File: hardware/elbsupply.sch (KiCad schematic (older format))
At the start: 82 parts, among them CON1 AVR-ISP-6, IC1 ATMEGA8-AI, P1 OUT_POS, P2 OUT_GND, P3 POWER_IN, Q1 KST2907A, SW1 SW_L, SW2 SW_R, SW3 SW_OE, SW4 SW_MD, U1 LM393, U2 TPS54331DDA, U3 LT1490, U4 LM358, U5 TS78L05CS, U6 LT3083

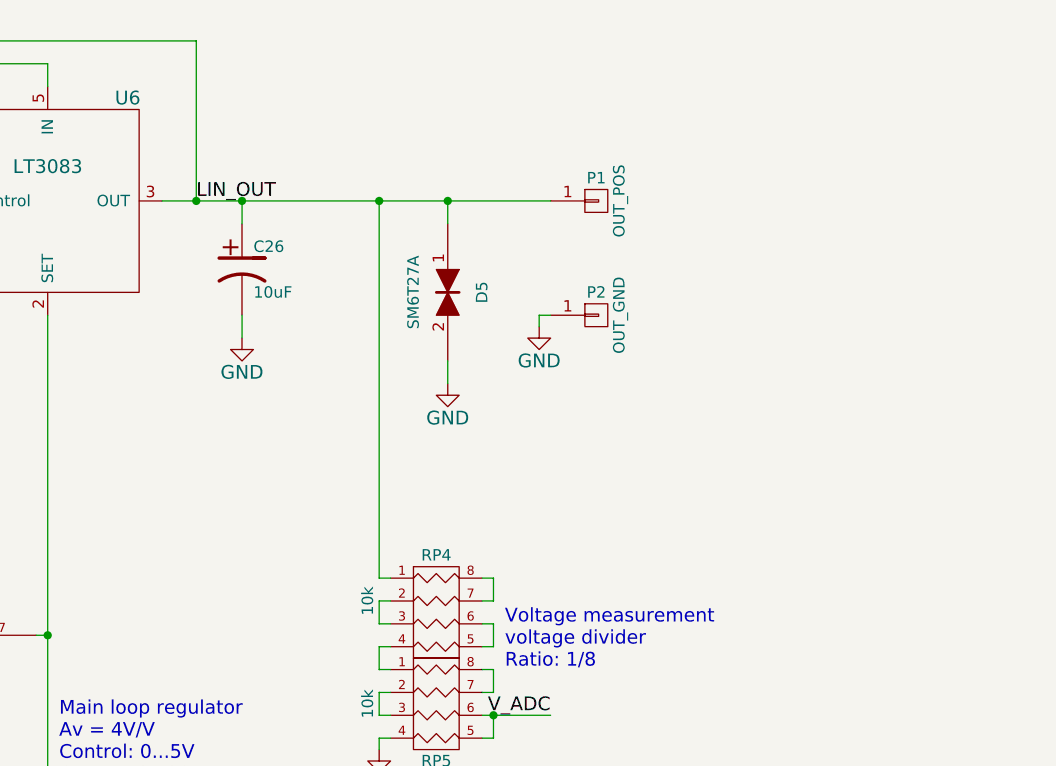
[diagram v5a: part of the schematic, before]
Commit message: quickly added LM334 constant current sink to ensure stable operation of LT3083
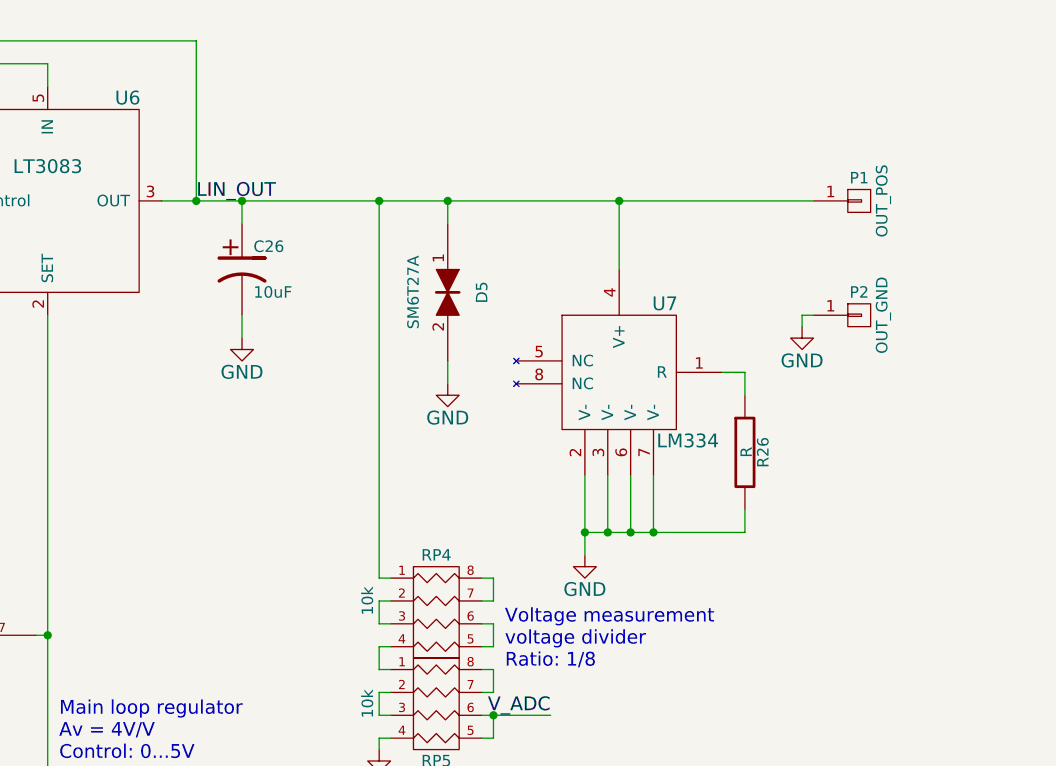
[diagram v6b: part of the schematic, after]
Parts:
- added R26: R, Resistors_SMD:R_0603_HandSoldering, symbol R
- added U7: LM334, devthrash_KICAD:SO8, symbol LM334
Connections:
- net GND: now also R26.2, U7.2 (V-), U7.3 (V-), U7.6 (V-), U7.7 (V-)
- net LIN_OUT: now also U7.4 (V+)
- new net: R26.1, U7.1 (R)
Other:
- moved on the sheet: P1, P2
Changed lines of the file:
@@
 LIBS:lt3083
 LIBS:tps54331dda
+LIBS:LM334
 LIBS:elbsupply-cache
 EELAYER 25 0
@@
 L GND #PWR044
 U 1 1 54ED932C
-P 13350 1950
-F 0 "#PWR044" H 13350 1700 60  0001 C CNN
-F 1 "GND" H 13350 1800 60  0000 C CNN
-F 2 "" H 13350 1950 60  0000 C CNN
-F 3 "" H 13350 1950 60  0000 C CNN
-	1    13350 1950
+P 14500 1950
+F 0 "#PWR044" H 14500 1700 60  0001 C CNN
+F 1 "GND" H 14500 1800 60  0000 C CNN
+F 2 "" H 14500 1950 60  0000 C CNN
+F 3 "" H 14500 1950 60  0000 C CNN
+	1    14500 1950
 	1    0    0    -1
 $EndComp
@@
 	14150 8400 13800 8400
 Wire Wire Line
-	11700 1400 13400 1400
+	11700 1400 14550 1400
 Wire Wire Line
 	12050 2000 12050 1900
@@
 	7050 5750 7050 5700
 Wire Wire Line
-	13400 1900 13350 1900
-Wire Wire Line
-	13350 1900 13350 1950
+	14550 1900 14500 1900
+Wire Wire Line
+	14500 1900 14500 1950
 Wire Wire Line
 	7850 3300 7750 3300
@@
 L CONN_01X01 P1
 U 1 1 54F668BE
-P 13600 1400
-F 0 "P1" H 13600 1500 50  0000 C CNN
-F 1 "OUT_POS" V 13700 1400 50  0000 C CNN
-F 2 "devthrash_KICAD:SKS-PK10A" H 13600 1400 60  0001 C CNN
-F 3 "" H 13600 1400 60  0000 C CNN
-	1    13600 1400
+P 14750 1400
+F 0 "P1" H 14750 1500 50  0000 C CNN
+F 1 "OUT_POS" V 14850 1400 50  0000 C CNN
+F 2 "devthrash_KICAD:SKS-PK10A" H 14750 1400 60  0001 C CNN
+F 3 "" H 14750 1400 60  0000 C CNN
+	1    14750 1400
 	1    0    0    -1
 $EndComp
@@
 L CONN_01X01 P2
 U 1 1 54F6697F
-P 13600 1900
-F 0 "P2" H 13600 2000 50  0000 C CNN
-F 1 "OUT_GND" V 13700 1900 50  0000 C CNN
-F 2 "devthrash_KICAD:SKS-PK10A" H 13600 1900 60  0001 C CNN
-F 3 "" H 13600 1900 60  0000 C CNN
-	1    13600 1900
+P 14750 1900
+F 0 "P2" H 14750 2000 50  0000 C CNN
+F 1 "OUT_GND" V 14850 1900 50  0000 C CNN
+F 2 "devthrash_KICAD:SKS-PK10A" H 14750 1900 60  0001 C CNN
+F 3 "" H 14750 1900 60  0000 C CNN
+	1    14750 1900
 	1    0    0    -1
 $EndComp
@@
 Text Label 14150 9200 2    60   ~ 0
 SW_OE
+$Comp
+L LM334 U7
+U 1 1 54FCA3D9
+P 13700 2150
+F 0 "U7" H 13900 2450 60  0000 C CNN
+F 1 "LM334" H 14000 1850 60  0000 C CNN
+F 2 "devthrash_KICAD:SO8" H 14200 2500 60  0001 C CNN
+F 3 "" H 14200 2500 60  0000 C CNN
+	1    13700 2150
+	1    0    0    -1
+$EndComp
+$Comp
+L R R26
+U 1 1 54FCA896
+P 14250 2500
+F 0 "R26" V 14330 2500 50  0000 C CNN
+F 1 "R" V 14257 2501 50  0000 C CNN
+F 2 "Resistors_SMD:R_0603_HandSoldering" V 14180 2500 30  0001 C CNN
+F 3 "" H 14250 2500 30  0000 C CNN
+	1    14250 2500
+	1    0    0    -1
+$EndComp
+Wire Wire Line
+	13550 2600 13550 2950
+Wire Wire Line
+	13550 2850 14250 2850
+Wire Wire Line
+	14250 2850 14250 2750
+$Comp
+L GND #PWR074
+U 1 1 54FCAB2D
+P 13550 2950
+F 0 "#PWR074" H 13550 2700 60  0001 C CNN
+F 1 "GND" H 13550 2800 60  0000 C CNN
+F 2 "" H 13550 2950 60  0000 C CNN
+F 3 "" H 13550 2950 60  0000 C CNN
+	1    13550 2950
+	1    0    0    -1
+$EndComp
+Connection ~ 13550 2850
+Wire Wire Line
+	13650 2600 13650 2850
+Connection ~ 13650 2850
+Wire Wire Line
+	13750 2600 13750 2850
+Connection ~ 13750 2850
+Wire Wire Line
+	13850 2600 13850 2850
+Connection ~ 13850 2850
+Wire Wire Line
+	14150 2150 14250 2150
+Wire Wire Line
+	14250 2150 14250 2250
+Wire Wire Line
+	13700 1400 13700 1700
+Connection ~ 13700 1400
 $EndSCHEMATC

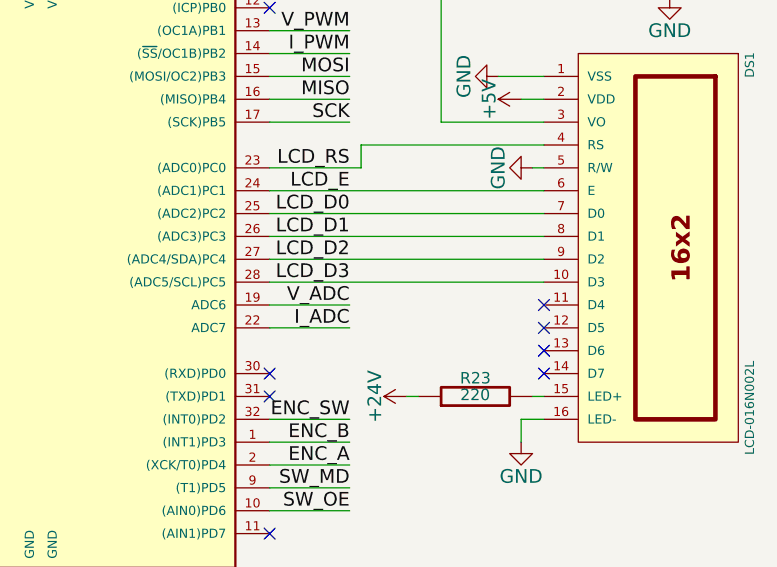
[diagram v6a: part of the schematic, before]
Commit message: made a mistake in LCD pinout, fixed in schematic, needs to be fixed on revision B board
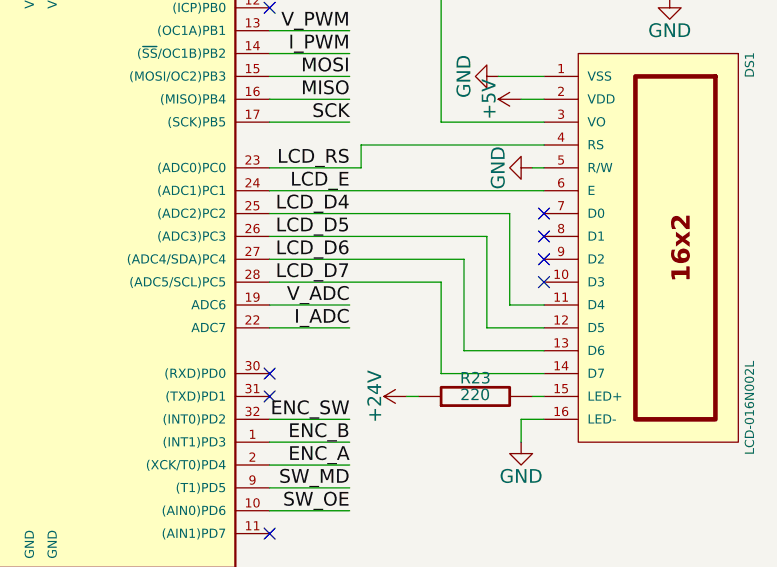
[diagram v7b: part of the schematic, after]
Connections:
- net LCD_D4: now reaches DS1.11 (D4)
- net LCD_D4: now also IC1.25 ((ADC2)PC2)
- net LCD_D5: now reaches DS1.12 (D5)
- net LCD_D5: now also IC1.26 ((ADC3)PC3)
- net LCD_D6: now reaches DS1.13 (D6)
- net LCD_D6: now also IC1.27 ((ADC4/SDA)PC4)
- net LCD_D7: now reaches DS1.14 (D7)
- net LCD_D7: now also IC1.28 ((ADC5/SCL)PC5)
- net LCD_D0: no longer names the net of DS1.7 (D0)
- net LCD_D0: no longer IC1.25 ((ADC2)PC2)
- net LCD_D1: no longer names the net of DS1.8 (D1)
- net LCD_D1: no longer IC1.26 ((ADC3)PC3)
- net LCD_D2: no longer names the net of DS1.9 (D2)
- net LCD_D2: no longer IC1.27 ((ADC4/SDA)PC4)
- net LCD_D3: no longer names the net of DS1.10 (D3)
- net LCD_D3: no longer IC1.28 ((ADC5/SCL)PC5)
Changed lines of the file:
@@
 	0    1    1    0
 $EndComp
-NoConn ~ 15000 8600
-NoConn ~ 15000 8500
-NoConn ~ 15000 8400
-NoConn ~ 15000 8300
 $Comp
 L POT RV1
@@
 LCD_E
 Text Label 14150 7900 2    60   ~ 0
-LCD_D0
+LCD_D4
 Text Label 14150 8000 2    60   ~ 0
-LCD_D1
+LCD_D5
 Text Label 14150 8100 2    60   ~ 0
-LCD_D2
+LCD_D6
 Text Label 14150 8200 2    60   ~ 0
-LCD_D3
+LCD_D7
 $Comp
 L GND #PWR016
@@
 	13800 7800 15000 7800
 Wire Wire Line
-	13800 7900 15000 7900
-Wire Wire Line
-	13800 8000 15000 8000
-Wire Wire Line
-	13800 8100 15000 8100
-Wire Wire Line
-	13800 8200 15000 8200
-Wire Wire Line
 	14200 7700 14200 7600
 Wire Wire Line
@@
 	13700 1400 13700 1700
 Connection ~ 13700 1400
+NoConn ~ 15000 7900
+NoConn ~ 15000 8000
+NoConn ~ 15000 8100
+NoConn ~ 15000 8200
+Wire Wire Line
+	15000 8300 14850 8300
+Wire Wire Line
+	14850 8300 14850 7900
+Wire Wire Line
+	14850 7900 13800 7900
+Wire Wire Line
+	13800 8000 14750 8000
+Wire Wire Line
+	14750 8000 14750 8400
+Wire Wire Line
+	14750 8400 15000 8400
+Wire Wire Line
+	15000 8500 14650 8500
+Wire Wire Line
+	14650 8500 14650 8100
+Wire Wire Line
+	14650 8100 13800 8100
+Wire Wire Line
+	13800 8200 14550 8200
+Wire Wire Line
+	14550 8200 14550 8600
+Wire Wire Line
+	14550 8600 15000 8600
 $EndSCHEMATC
